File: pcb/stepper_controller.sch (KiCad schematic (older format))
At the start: 13 parts, among them P1 DBNC_INPUT, P2 DRIVE, P3 +24VDC, P4 INT_STEPPER, P5 INT_TONE, U1 MAX6817

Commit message: Major changes to prepare for pcb mounted stepper driver.
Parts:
- removed C1, C2: 10uF, symbol C-RESCUE-stepper_controller
- removed C3: 0.1uF, symbol C-RESCUE-stepper_controller
- removed P1: DBNC_INPUT, symbol CONN_4
- removed P2: DRIVE, symbol CONN_4
- removed P3: +24VDC, symbol CONN_2
- removed P4: INT_STEPPER, symbol CONN_2
- removed P5: INT_TONE, symbol CONN_2
- removed R1: 118, symbol R-RESCUE-stepper_controller
- removed REG1: CONV_DC_DC, symbol CONV_DC_DC
- removed SHIELD1: ARDUINO_MEGA_SHIELD_FULL, symbol ARDUINO_MEGA_SHIELD_FULL
- removed SP1: SPEAKER, symbol SPEAKER
- added ARDUINO1: ARDUINO_MEGA, stepper_controller:ARDUINO_MEGA_SHIELD, symbol ARDUINO_MEGA
- added C1, C2, C3, C6, C7, C8, C9: 10uF, stepper_controller:SM1210, symbol 10uF
- added C4, C5: 0.1uF, stepper_controller:SM1210, symbol 0.1uF
- added D1: LED_24V, stepper_controller:LED_555-3XXX, symbol LED_24V
- added E1: ENCODER_C14, stepper_controller:Micro-MaTch_6_SMD, symbol ENCODER_C14
- added P1: PWR_JACK_2.5x5.5, stepper_controller:DCJACK_2PIN_HIGHCURRENT, symbol PWR_JACK_2.5x5.5
- added P2: HEADER_01X03, stepper_controller:Header_3_Pin, symbol HEADER_01X03
- added P3: BNC_DOUBLE_RA, stepper_controller:BNC_DOUBLE, symbol BNC_DOUBLE_RA
- added P4, P5: HEADER_01X03_SMD_RA, stepper_controller:Header_3_Pin_SMD_RA, symbol HEADER_01X03_SMD_RA
- added R1, R2: 5.11k, stepper_controller:SM1210, symbol 5.11k
- added R3, R4, R5, R6: 150, stepper_controller:SM1210, symbol 150
- added RCD1, RCD2, RCD3, RCD4: RCD-24, stepper_controller:RCD-24, symbol RCD-24
- added REG1: CONV_DC_DC_12V_1A, stepper_controller:DC_DC_CONV_R78C, symbol CONV_DC_DC_12V_1A
- added S1: HEADER_01X02_SHR, stepper_controller:Header_Shrouded_2_Pin, symbol HEADER_01X02_SHR
- added SW1: DPST_SERIES_M, stepper_controller:DPST_SERIES_M, symbol DPST_SERIES_M
- added SW2: KT_SWITCH, stepper_controller:KT_SWITCH, symbol KT_SWITCH
- added T1, T2, T3, T4: TERM_BLK_ANG_2_PIN, stepper_controller:TERM_BLK_ANG_2_PIN, symbol TERM_BLK_ANG_2_PIN
- added U2: MAX6817, stepper_controller:MAX6817, symbol MAX6817
- added U3, U4, U5, U6: SSR_DC_6PIN, stepper_controller:ASSR-1611, symbol SSR_DC_6PIN
- U1: footprint (none) -> stepper_controller:MAX6817; Description (none) -> IC DEBOUNCER SWITCH DUAL SOT23-6; PartNumber (none) -> MAX6817EUT+TCT-ND; Vendor (none) -> digikey
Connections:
- net labels added: +5VD, BNC_A, BNC_B, BTN, D_BTN, D_ENC_BTN, D_LIGHTS, D_SWITCH, ENABLE_0, ENABLE_1, ENABLE_2, ENABLE_3, ENC_A, ENC_B, ENC_BTN, IN_0+, IN_1+, IN_2+, IN_3+, LED_PWR, LIGHTS, OUT_0+, OUT_0-, OUT_1+, OUT_1-, OUT_2+, OUT_2-, OUT_3+, OUT_3-, PWM_0, PWM_1, PWM_2, PWM_3, RX0, RX2, SWITCH, TX0, TX2, TX3, V_IN
- net labels removed: DIR, ENABLE, INT_STEPPER, INT_STEPPER_DEBOUNCED, INT_TONE, INT_TONE_DEBOUNCED, SPEAKER, STEP, VIN
- wire segments 60 -> 170
- no-connect marks 74 -> 63

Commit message: Use power_switch_controller as base for pcb.
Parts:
- removed C3, C6, C7, C8, C9: 10uF, stepper_controller:SM1210, symbol 10uF
- removed E1: ENCODER_C14, stepper_controller:Micro-MaTch_6_SMD, symbol ENCODER_C14
- removed P2: HEADER_01X03, stepper_controller:Header_3_Pin, symbol HEADER_01X03
- removed P3: BNC_DOUBLE_RA, stepper_controller:BNC_DOUBLE, symbol BNC_DOUBLE_RA
- removed R1, R2: 5.11k, stepper_controller:SM1210, symbol 5.11k
- removed R3, R4, R5, R6: 150, stepper_controller:SM1210, symbol 150
- removed RCD1, RCD2, RCD3, RCD4: RCD-24, stepper_controller:RCD-24, symbol RCD-24
- removed S1: HEADER_01X02_SHR, stepper_controller:Header_Shrouded_2_Pin, symbol HEADER_01X02_SHR
- removed SW1: DPST_SERIES_M, stepper_controller:DPST_SERIES_M, symbol DPST_SERIES_M
- removed SW2: KT_SWITCH, stepper_controller:KT_SWITCH, symbol KT_SWITCH
- removed T1, T2, T3, T4: TERM_BLK_ANG_2_PIN, stepper_controller:TERM_BLK_ANG_2_PIN, symbol TERM_BLK_ANG_2_PIN
- removed U1, U2: MAX6817, stepper_controller:MAX6817, symbol MAX6817
- removed U3, U4, U5, U6: SSR_DC_6PIN, stepper_controller:ASSR-1611, symbol SSR_DC_6PIN
- added C1: 10uF, stepper_controller:SM1210, symbol 10uF
- added C6, C7: 0.1uF, stepper_controller:SM1210, symbol 0.1uF
- added D10, D11, D12, D13, D14, D15, D16, D17, D18, D19, D2, D20, D21, D22, D23, D24, D25, D26, D27, D28, D29, D3, D30, D31, D32, D33, D4, D5, D6, D7, D8, D9: LED_24V, stepper_controller:LED_555-3XXX, symbol LED_24V
- added P10, P11, P8, P9: HEADER_02X08_SMD, stepper_controller:HEADER_02x08_SMD, symbol HEADER_02X08_SMD
- added P2, P3: HEADER_01X03_SMD_RA, stepper_controller:Header_3_Pin_SMD_RA, symbol HEADER_01X03_SMD_RA
- added P6: HEADER_01X02_SMD_RA, stepper_controller:Header_2_Pin_SMD_RA, symbol HEADER_01X02_SMD_RA
- added P7: BNC_DOUBLE_RA, stepper_controller:BNC_DOUBLE, symbol BNC_DOUBLE_RA
- added SW1: SPST_SLIDE_AS, stepper_controller:SPST_SLIDE_AS, symbol SPST_SLIDE_AS
- added U1, U2, U3, U4: TLE7230R, stepper_controller:PG-DSO-36, symbol TLE7230R
- renumbered C1 to C2, C2 to C3
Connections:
- net labels added: CS, MISO, MOSI, OUT0, OUT1, OUT10, OUT11, OUT12, OUT13, OUT14, OUT15, OUT16, OUT17, OUT18, OUT19, OUT2, OUT20, OUT21, OUT22, OUT23, OUT24, OUT25, OUT26, OUT27, OUT28, OUT29, OUT3, OUT30, OUT31, OUT4, OUT5, OUT6, OUT7, OUT8, OUT9, RESET, RX1, RX3, SCK, SO1, SO2, SO3, TX1
- net labels removed: BTN, D_BTN, D_ENC_BTN, D_LIGHTS, D_SWITCH, ENABLE_0, ENABLE_1, ENABLE_2, ENABLE_3, ENC_A, ENC_B, ENC_BTN, IN_0+, IN_1+, IN_2+, IN_3+, LIGHTS, OUT_0+, OUT_0-, OUT_1+, OUT_1-, OUT_2+, OUT_2-, OUT_3+, OUT_3-, PWM_0, PWM_1, PWM_2, PWM_3, SWITCH
- wire segments 170 -> 313
- no-connect marks 63 -> 73
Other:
- moved on the sheet: C2, C3, D1, P1, REG1

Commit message: Progress towards pcb 1.0.
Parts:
- removed C4, C5, C6, C7: 0.1uF, stepper_controller:SM1210, symbol 0.1uF
- removed D10, D11, D12, D13, D14, D15, D16, D17, D18, D19, D2, D20, D21, D22, D23, D24, D25, D26, D27, D28, D29, D3, D30, D31, D32, D33, D4, D5, D6, D7, D8, D9: LED_24V, stepper_controller:LED_555-3XXX, symbol LED_24V
- removed P10, P11, P8, P9: HEADER_02X08_SMD, stepper_controller:HEADER_02x08_SMD, symbol HEADER_02X08_SMD
- removed U1, U2, U3, U4: TLE7230R, stepper_controller:PG-DSO-36, symbol TLE7230R
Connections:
- no-connect marks 73 -> 65

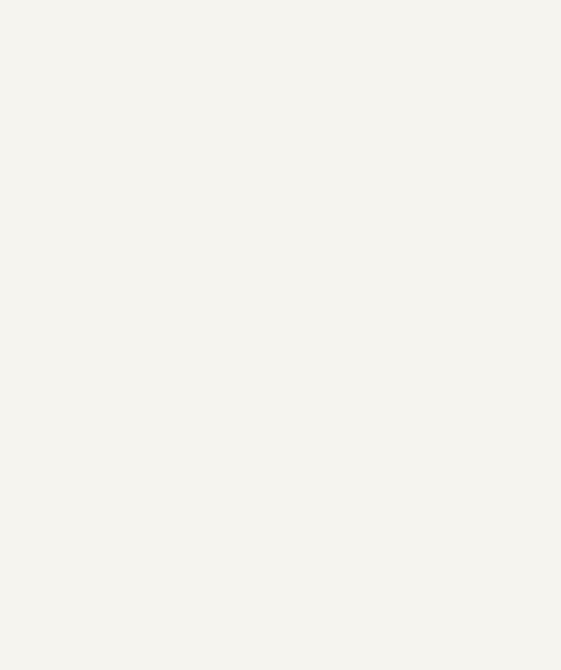
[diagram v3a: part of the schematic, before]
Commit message: Added IM483H to schematic.
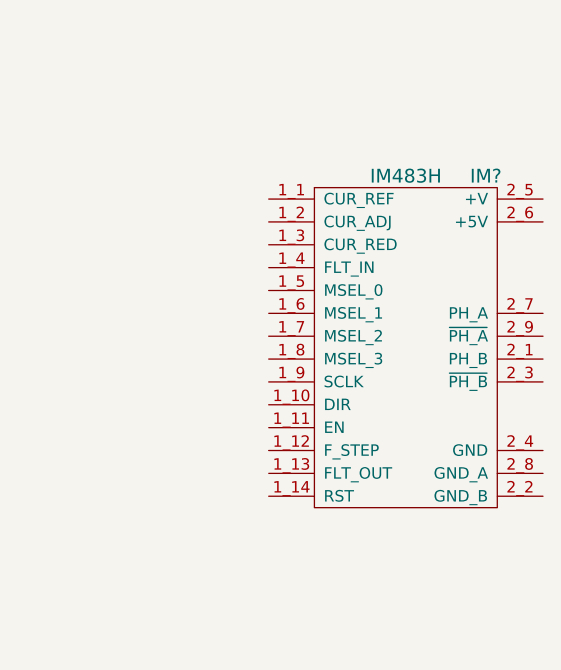
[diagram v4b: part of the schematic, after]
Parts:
- added IM?: IM483H, stepper_controller:IM483H_IM805H_PR-22, symbol IM483H
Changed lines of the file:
@@
 Text Label 1000 5150 0    60   ~ 0
 RESET
+$Comp
+L IM483H IM?
+U 1 1 56DE1C59
+P 7850 2250
+F 0 "IM?" H 8200 3000 60  0000 C CNN
+F 1 "IM483H" H 7850 3000 60  0000 C CNN
+F 2 "stepper_controller:IM483H_IM805H_PR-22" H 7850 3300 60  0001 C CNN
+F 3 "" H 8150 3000 60  0000 C CNN
+F 4 "schneider" H 7850 3400 60  0001 C CNN "Vendor"
+F 5 "IM483H_Plus" H 7850 3500 60  0001 C CNN "PartNumber"
+F 6 "Microstepping driver 12-48 VDC 3.0 amps RMS" H 7850 3600 60  0001 C CNN "Description"
+	1    7850 2250
+	1    0    0    -1
+$EndComp
 $EndSCHEMATC

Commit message: Progress towards firmware update.
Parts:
- added R1: 1.69k, stepper_controller:SM1210, symbol 1.69k
- added R2: 316, stepper_controller:SM1210, symbol 316
- gave numbers to parts that had none: 1
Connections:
- net labels added: DIR, ENABLE, MSEL_0, MSEL_1, MSEL_2, MSEL_3, PHASE_A, PHASE_B, STEP, ~PHASE_A, ~PHASE_B
- net labels removed: CS, MISO, MOSI, RESET, SCK
- wire segments 67 -> 94
- no-connect marks 65 -> 69
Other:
- moved on the sheet: IM1
